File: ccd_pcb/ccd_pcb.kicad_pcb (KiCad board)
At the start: 4 copper layers, 184 parts, among them J1 GS3, J2 GS3, J3 GS3, J4 PMODx2 North, J6 PMOD-Host-x1-GPIO, J7 GS3, J8 Extension North, J9 Extension South, U1 74LVC1T45GW, U2 BMX055, U3 TXS0108E, U4 TXS0108E, U5 TXS0108E, U6 ADP150-2.8, U7 MCP1727-1V8, U8 MCP1727-3V3, U9 ar0330CM

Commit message: update
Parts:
- removed C35, C36, C40, C41: 1µ, Capacitors_SMD:C_0402
- added R110: 15k, Resistors_SMD:R_0603_HandSoldering, F.Cu at (79.5, 41.9)
- added R111: 15k, Resistors_SMD:R_0603_HandSoldering, F.Cu at (76.1, 109.8)
- added R112: 15k, Resistors_SMD:R_0603_HandSoldering, F.Cu at (84.2, 41.9)
- added R113: 15k, Resistors_SMD:R_0603_HandSoldering, F.Cu at (76.3, 112.4)
- C30, C31: value 1µ -> .1µF
- moved C31 206.8 mm to (275.7, 44.0)
- moved C30 195.1 mm to (272.9, 44.4)
- moved C2 8.82 mm to (249.5, 33.7), turned to 180 degrees
- moved U2 0.64 mm to (253.0, 33.7), turned to 180 degrees
- turned U9 to 180 degrees
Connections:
- C31 pad 1: VDDIO_35 -> /5V
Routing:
- net /5V: track 0.00 -> 2.30 mm

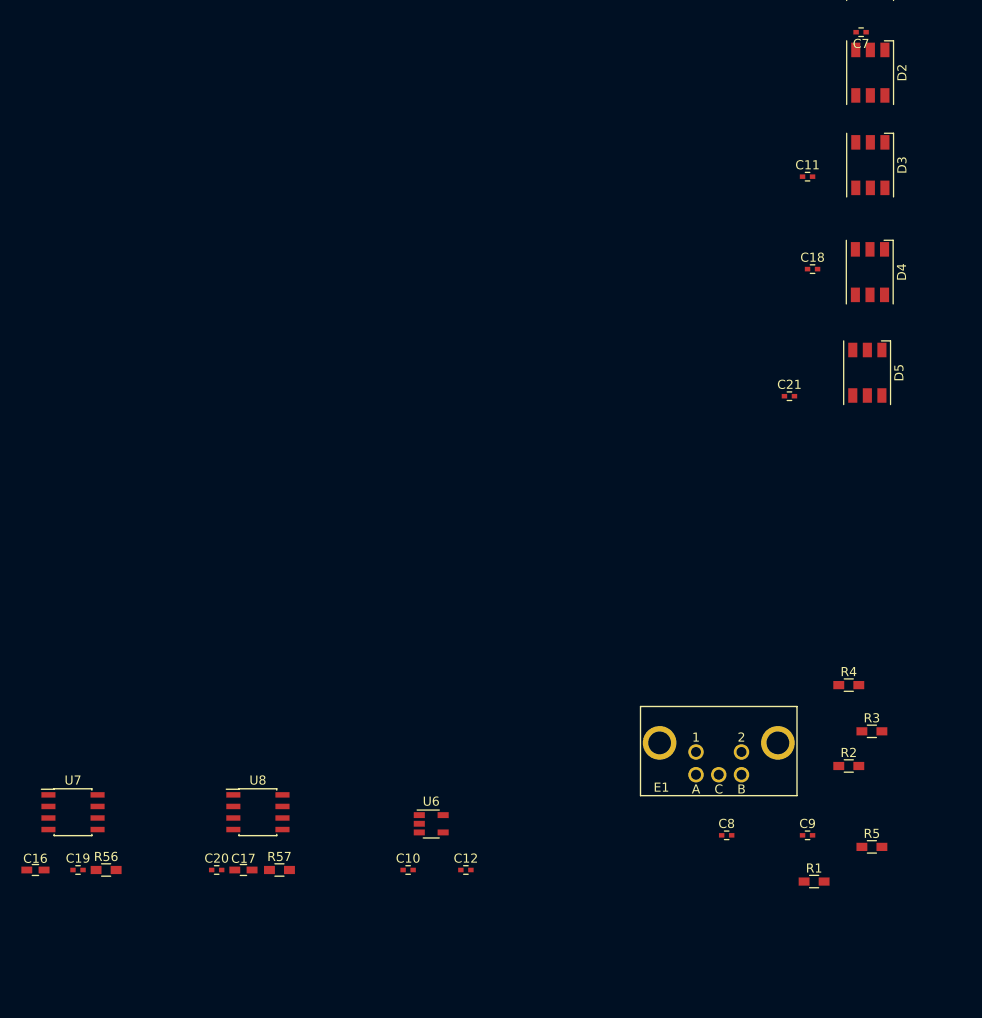
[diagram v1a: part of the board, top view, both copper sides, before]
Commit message: better model of zturn lite
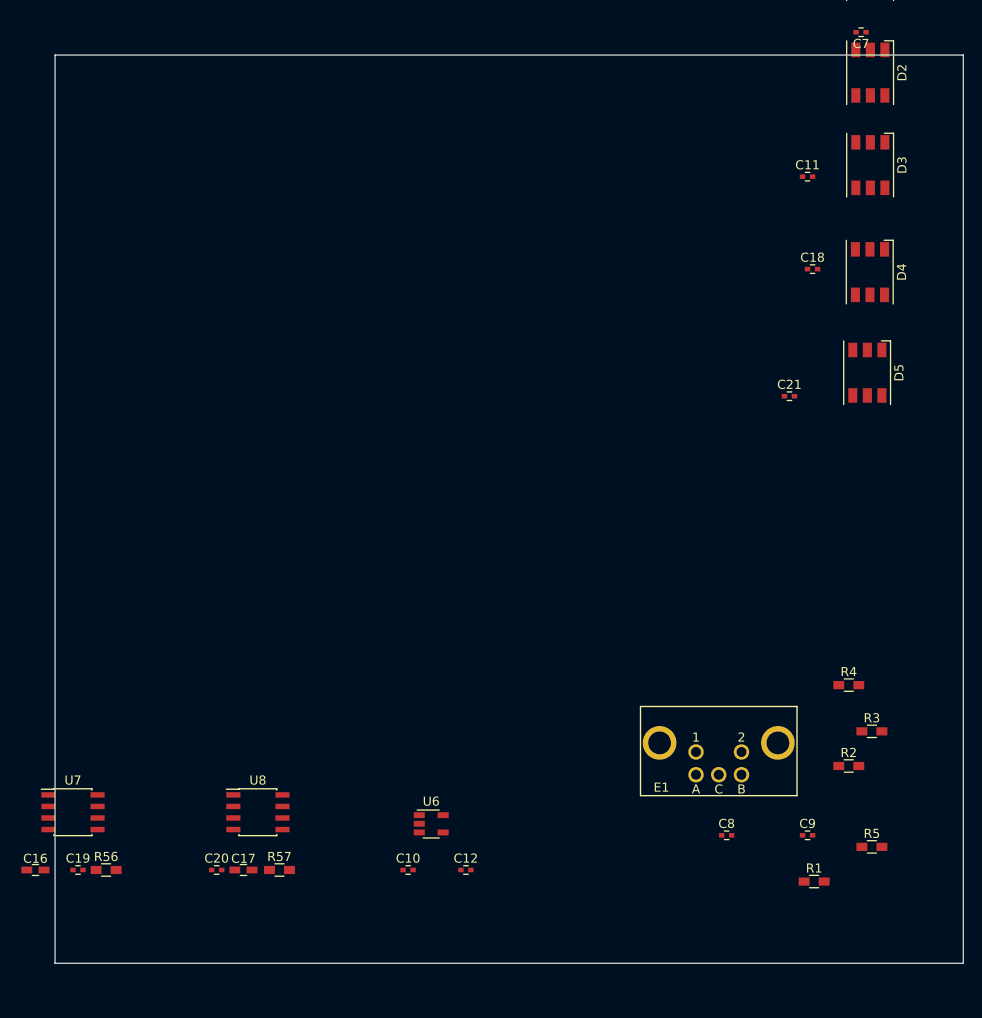
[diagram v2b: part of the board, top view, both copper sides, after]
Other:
- board outline added: 99.8 x 99.8 mm
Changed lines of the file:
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@@
   (general
     (links 369)
-    (no_connects 366)
-    (area 0 0 0 0)
+    (no_connects 369)
+    (area 19.959429 11.292999 277.477667 193.483904)
     (thickness 1.6)
-    (drawings 0)
+    (drawings 4)
     (tracks 3)
     (zones 0)
@@
     (pad_drill 3.124)
     (pad_to_mask_clearance 0)
-    (aux_axis_origin 35 39)
+    (aux_axis_origin 44.196 30.861)
     (visible_elements FFFFEF7F)
     (pcbplotparams
@@
     )
   )
+  (gr_line (start 282.448 172.466) (end 282.448 72.644) (layer Edge.Cuts) (width 0.1))
+  (gr_line (start 182.626 172.466) (end 282.448 172.466) (layer Edge.Cuts) (width 0.1))
+  (gr_line (start 182.626 72.644) (end 182.626 172.466) (layer Edge.Cuts) (width 0.1))
+  (gr_line (start 182.626 72.644) (end 282.448 72.644) (layer Edge.Cuts) (width 0.1))
   (segment (start 139.5435 84.74) (end 139.642 84.74) (width 0.6) (layer F.Cu) (net 2))
   (segment (start 137.871 83.47) (end 138.2735 83.47) (width 0.25) (layer F.Cu) (net 2))

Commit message: update
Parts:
- added REF**: MountingHole_3.2mm_M3, Mounting_Holes:MountingHole_3.2mm_M3, F.Cu at (303.8, -85.3)
- added REF**: MountingHole_3.2mm_M3, Mounting_Holes:MountingHole_3.2mm_M3, F.Cu at (219.9, -85.3)
- added REF**: MountingHole_3.2mm_M3, Mounting_Holes:MountingHole_3.2mm_M3, F.Cu at (219.9, -29.5)
- added REF**: MountingHole_3.2mm_M3, Mounting_Holes:MountingHole_3.2mm_M3, F.Cu at (303.8, -29.5)
- U9: moved to B.Cu
- moved A1 223.3 mm to (300.6, -55.1), turned to 270 degrees
- moved R108 198.7 mm to (292.2, -66.9)
- moved R109 198.7 mm to (292.2, -70.7)
- moved C47 145.5 mm to (259.1, -62.1), turned to 270 degrees
- moved C45 144.7 mm to (266.6, -59.4), turned to 180 degrees
- moved C38 137.4 mm to (266.5, -53.8), turned to 180 degrees
- moved C29 132.4 mm to (266.3, -62.2), turned to 270 degrees
- moved C39 127.8 mm to (264.7, -62.2), turned to 270 degrees
- moved C37 119.9 mm to (257.3, -56.2)
- moved C27 115.1 mm to (257.3, -57.0)
- moved C32 112.7 mm to (257.9, -43.9), turned to 180 degrees
- moved C23 111.4 mm to (269.2, -42.0)
- moved C33 111.4 mm to (243.8, -35.7)
- moved C43 111.4 mm to (243.8, -31.8)
- moved C46 111.4 mm to (243.8, -28.0)
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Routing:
- net /5V: track 2.30 -> 0.00 mm
- net (no net): track 0.00 -> 2.30 mm
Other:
- board size 99.8 x 99.8 mm -> 90.9 x 90.9 mm

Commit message: update
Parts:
- moved J9 281.1 mm to (278.8, -95.5), turned to 180 degrees
- moved R111 280.5 mm to (275.8, -87.2)
- moved R113 280.5 mm to (276.0, -84.6)
- moved C15 263.2 mm to (225.9, -47.4)
- moved J6 262.2 mm to (219.0, -44.3), turned to 180 degrees
- moved C6 261.9 mm to (237.5, -52.0)
- moved U5 259.7 mm to (231.6, -49.2), turned to 180 degrees
- moved C14 250.9 mm to (278.3, -21.7)
- moved C12 250.1 mm to (155.0, -77.1), turned to 90 degrees
- moved U4 249.3 mm to (283.4, -29.4)
- moved C5 244.9 mm to (279.2, -30.3)
- moved C10 242.2 mm to (155.0, -70.7), turned to 90 degrees
- moved U6 242.0 mm to (149.9, -73.3), turned to 90 degrees
- moved R57 225.0 mm to (155.0, -56.6), turned to 90 degrees
- moved J4 221.9 mm to (251.6, -16.8)
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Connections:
- A1 pad 10: LVDSs2_P -> LVDSn0_P
- A1 pad 100: PMOD3_S -> SLVSC_N
- A1 pad 103: CCD_CLK -> PMOD3_S
- A1 pad 104: PMOD4_S -> SLVS1_P
- A1 pad 105: RESET -> PMOD2_S
- A1 pad 106: PMOD5_S -> SLVS1_N
- A1 pad 107: S_CLK -> PMOD1_S
- A1 pad 108: PMOD6_S -> SLVS0_P
- A1 pad 109: S_DATA -> PMOD0_S
- A1 pad 11: LVDSn5_N -> LVDSs0_N
- A1 pad 110: PMOD7_S -> SLVS0_N
- A1 pad 12: LVDSs2_N -> LVDSn0_N
- A1 pad 13: LVDSn4_P -> LVDSs1_P
- A1 pad 14: LVDSs1_P -> LVDSn1_P
- A1 pad 15: LVDSn4_N -> LVDSs1_N
- A1 pad 16: LVDSs1_N -> LVDSn1_N
- A1 pad 21: LVDSn3_P -> LVDSs2_P
- A1 pad 22: LVDSs0_P -> LVDSn2_P
- A1 pad 23: LVDSn3_N -> LVDSs2_N
- A1 pad 24: LVDSs0_N -> LVDSn2_N
- A1 pad 25: LVDSn2_P -> LVDSs3_P
- A1 pad 26: LVDSs4_P -> LVDSn3_P
- A1 pad 27: LVDSn2_N -> LVDSs3_N
- A1 pad 28: LVDSs4_N -> LVDSn3_N
- A1 pad 3: SDA_N -> SCL_S
- A1 pad 31: LVDSn1_P -> LVDSs4_P
- A1 pad 32: LVDSs5_P -> LVDSn4_P
- A1 pad 33: LVDSn1_N -> LVDSs4_N
- A1 pad 34: LVDSs5_N -> LVDSn4_N
- A1 pad 35: LVDSn0_P -> LVDSs5_P
- A1 pad 36: LVDSs3_P -> LVDSn5_P
- A1 pad 37: LVDSn0_N -> LVDSs5_N
- A1 pad 38: LVDSs3_N -> LVDSn5_N
- A1 pad 4: SCL_S -> SDA_N
- A1 pad 41: IO6_N -> IO0_S
- A1 pad 42: IO6_S -> IO0_N
- A1 pad 43: IO7_N -> IO1_S
- A1 pad 44: IO7_S -> IO1_N
- A1 pad 45: IO4_N -> IO2_S
- A1 pad 46: IO4_S -> IO2_N
- A1 pad 47: IO5_N -> IO3_S
- A1 pad 48: IO5_S -> IO3_N
- A1 pad 5: SCL_N -> SDA_S
- A1 pad 51: IO2_N -> IO4_S
- A1 pad 52: IO3_S -> IO4_N
- A1 pad 53: IO3_N -> IO5_S
- A1 pad 54: IO2_S -> IO5_N
- A1 pad 55: IO0_N -> IO6_S
- A1 pad 56: IO1_S -> IO6_N
- A1 pad 57: IO1_N -> IO7_S
- A1 pad 58: IO0_S -> IO7_N
- A1 pad 6: SDA_S -> SCL_N
- A1 pad 61: PMOD1_E -> PMOD2_E
- A1 pad 62: PMOD2_E -> PMOD1_E
- A1 pad 63: PMOD0_E -> PMOD3_E
- A1 pad 64: PMOD3_E -> PMOD0_E
- A1 pad 65: EN_S -> EN_B
- A1 pad 66: EN_B -> EN_S
- A1 pad 67: WS2812 -> EN_A
- A1 pad 68: EN_A -> WS2812
- A1 pad 71: SHUTTER -> PMOD7_N
- A1 pad 73: CCD_TRIGGER -> PMOD6_N
- A1 pad 74: PMOD0_N -> CCD_CLK
- A1 pad 75: SLVS0_P -> PMOD5_N
- A1 pad 76: PMOD1_N -> RESET
- A1 pad 77: SLVS0_N -> PMOD4_N
- A1 pad 78: PMOD2_N -> CCD_TRIGGER
- A1 pad 80: PMOD7_N -> SHUTTER
- A1 pad 83: SLVS1_P -> PMOD3_N
- A1 pad 84: PMOD6_N -> S_CLK
- A1 pad 85: SLVS1_N -> PMOD2_N
- A1 pad 86: PMOD5_N -> S_DATA
- A1 pad 87: SLVSC_P -> PMOD1_N
- A1 pad 88: PMOD4_N -> SLVS3_P
- A1 pad 89: SLVSC_N -> PMOD0_N
- A1 pad 9: LVDSn5_P -> LVDSs0_P
- A1 pad 90: PMOD3_N -> SLVS3_N
- A1 pad 93: SLVS2_P -> PMOD7_S
- A1 pad 94: PMOD0_S -> SLVS2_P
- A1 pad 95: SLVS2_N -> PMOD6_S
- A1 pad 96: PMOD1_S -> SLVS2_N
- A1 pad 97: SLVS3_P -> PMOD5_S
- A1 pad 98: PMOD2_S -> SLVSC_P
- A1 pad 99: SLVS3_N -> PMOD4_S
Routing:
- net SLVS3_N: track 0.00 -> 46.5 mm, vias 0 -> 1
- net SLVS3_P: track 0.00 -> 46.5 mm, vias 0 -> 1
- net SLVS2_P: track 0.00 -> 46.4 mm, vias 0 -> 1
- net SLVS2_N: track 0.00 -> 46.4 mm, vias 0 -> 1
- net SLVSC_N: track 0.00 -> 46.2 mm, vias 0 -> 1
- net SLVSC_P: track 0.00 -> 46.2 mm, vias 0 -> 1
- net SLVS1_P: track 0.00 -> 45.5 mm, vias 0 -> 1
- net SLVS1_N: track 0.00 -> 45.5 mm, vias 0 -> 1
- net SLVS0_N: track 0.00 -> 45.2 mm, vias 0 -> 1
- net SLVS0_P: track 0.00 -> 45.2 mm, vias 0 -> 1
- net (no net): track 2.30 -> 0.00 mm
- net VDDIO_34: vias 0 -> 2
- net /2V8: vias 0 -> 3
- net /1V8: vias 0 -> 5
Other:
- net class lvds: clearance 0.152 -> 0.13; trace_width 0.16 -> 0.13
- rule trace_min: 0.1524 -> 0.0889
- rule via_min_drill: 0.3 -> 0.2
- rule via_min_size: 0.6 -> 0.45
